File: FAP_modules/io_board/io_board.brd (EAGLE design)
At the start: 100 x 60 mm, 74 parts, among them IC1 STM32F051C8T6, IC2 EPM240-T100, IC3 24C08BSN, U2 OSCILLATORSMD

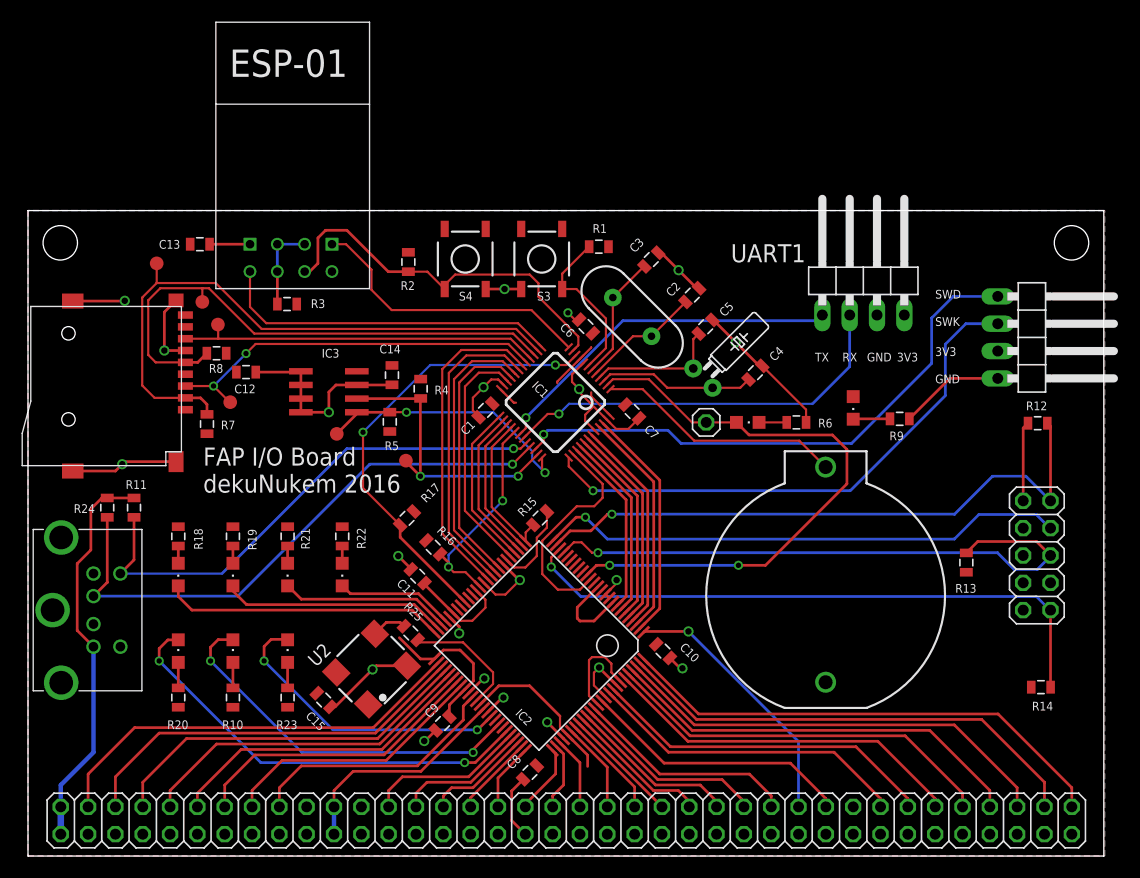
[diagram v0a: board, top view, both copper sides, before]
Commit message: WAIT and interrupt chaining on IO board
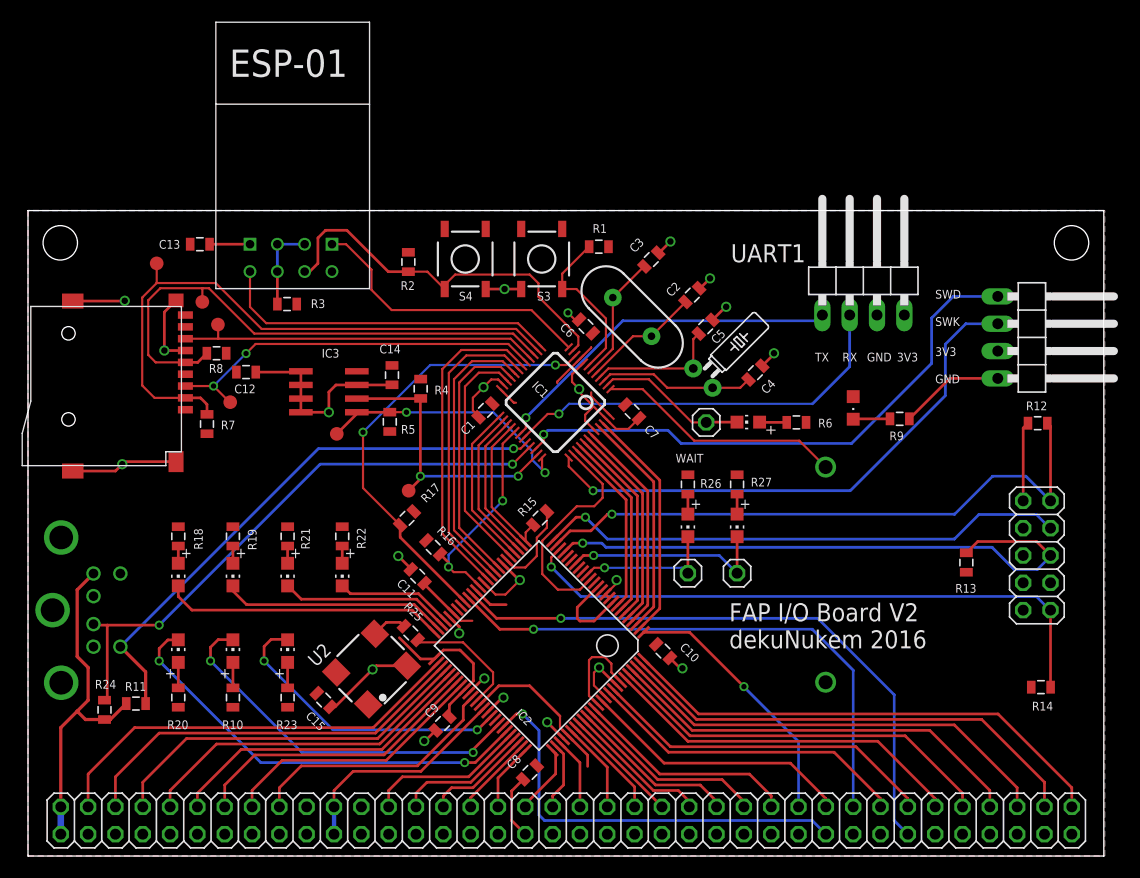
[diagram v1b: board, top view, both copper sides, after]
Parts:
- added JP5, JP6: (no value), pinhead:1X01
- added LED10, LED11: (no value), adafruit:CHIP-LED0805
- added R26, R27: (no value), SparkFun-Passives:0805
- LED1, LED3, LED4, LED5, LED6, LED7, LED8, LED9: device adafruit:CHIPLED_0805 -> adafruit:CHIP-LED0805
- U$1: value FAP_BUS -> FAP_BUS_FAP_BUS; device vga_pcb:2X38 -> cpu_board:FAP_BUS_2X38
- moved R24 18.8 mm to (7.11, 13.6), turned to 270 degrees
- moved R11 18.2 mm to (10.0, 14.2), turned to 180 degrees
- moved TP6 2.81 mm to (35.4, 34.0)
- moved LED1 0.06 mm to (67.0, 40.3), turned to 90 degrees
- flipped BAT1 to the bottom
- flipped U$2 to the bottom, turned to 270 degrees
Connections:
- new net N$100: IC2.41, U$1.NMI
- new net N$101: IC2.40, U$1.WAIT
- new net N$102: LED10.A, R26.2
- new net N$103: IC2.16, JP5.1, LED10.C
- new net N$104: LED11.A, R27.2
- new net N$105: IC2.19, JP6.1, LED11.C
- new net N$99: IC2.69, U$1.INTI
- net +3V3: now also R26.1, R27.1, R6.1
- net GND: no longer R6.1, U$1.GND@29, U$1.GND@32
- net N$23: now also U$1.INTO; no longer U$1.INT
- net N$73: now also LED1.C; no longer IC2.16, LED1.A
- net N$74: now also LED1.A; no longer LED1.C
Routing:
- net N$101: track 0.00 -> 56.6 mm, vias 0 -> 1
- net N$100: track 0.00 -> 51.2 mm, vias 0 -> 1
- net N$73: track 56.2 -> 14.0 mm, vias 2 -> 0
- net N$99: track 0.00 -> 39.8 mm, vias 0 -> 1
- net N$105: track 0.00 -> 19.5 mm, vias 0 -> 1
- net N$103: track 0.00 -> 13.3 mm, vias 0 -> 1
- net GND: track 146.7 -> 135.2 mm, vias 21 -> 23
- net +5V: track 37.1 -> 31.8 mm
- net N$65: track 48.6 -> 51.9 mm
- net N$104: track 0.00 -> 1.86 mm
- net N$102: track 0.00 -> 1.86 mm
- net N$66: track 54.3 -> 54.6 mm, vias 1 -> 2
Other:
- board text added: "FAP I/O Board V2 dekuNukem 2016"
- board text added: "WAIT"
- board text removed: "FAP I/O Board dekuNukem 2016"
